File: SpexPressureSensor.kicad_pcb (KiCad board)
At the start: 2 copper layers, 28 x 28 mm, 28 parts, among them P1 CONN_6, P2 NICHROME, P3 TC2030-CTX, Q1 IRLL3303PbF, U1 ST1480ABDR, U2 TPS769XX, U3 MKL03ZxxVFG4, U4 BMP180, U7 LT6105

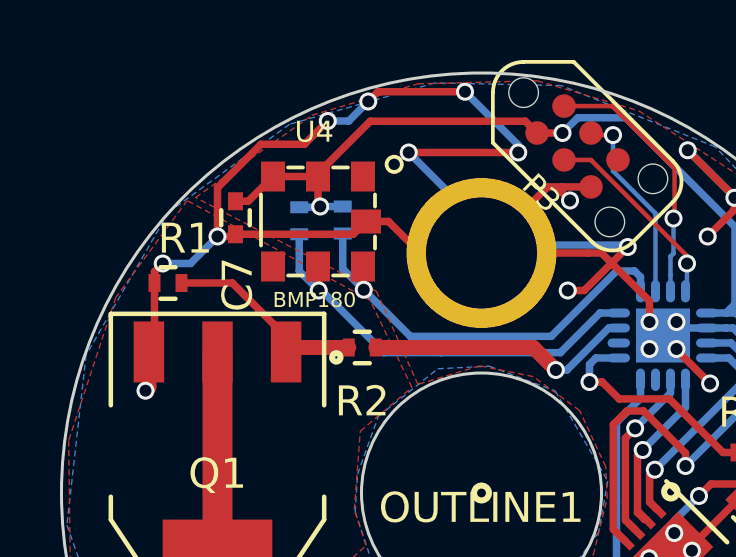
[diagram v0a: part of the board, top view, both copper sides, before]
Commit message: Changed the bmp180 for teh bme
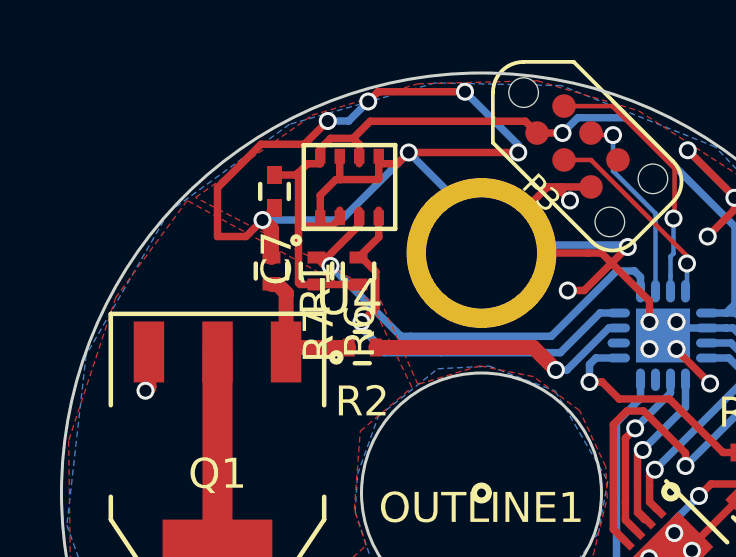
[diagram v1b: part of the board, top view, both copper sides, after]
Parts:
- C18: value C -> 1u
- R16, R18: value R -> 100
- R19: value R -> .02
- R20: value R -> 1000
- R6, R7: moved to F.Cu
- U4: value BMP180 -> BME280; footprint BMP180:LGA7-1.5-3.8X3.6MM -> bme280:LGA-8
- moved R1 3.47 mm to (113.0, 57.6), turned to 90 degrees
- moved R6 2.59 mm to (115.9, 57.6), turned to 90 degrees
- moved R7 1.91 mm to (114.5, 57.6), turned to 90 degrees
- moved C7 1.57 mm to (113.1, 55.0)
- moved U4 1.56 mm to (115.6, 54.8)
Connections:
- U4 pad 1: (no net) -> GND
- U4 pad 3: +3.3V -> Net-(R7-Pad2)
- U4 pad 4: (no net) -> Net-(R6-Pad2)
- U4 pad 5: Net-(R6-Pad2) -> GND
- U4 pad 6: Net-(R7-Pad2) -> +3.3V
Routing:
- net +3.3V: track 74.8 -> 79.3 mm, vias 6 -> 5
- net GND: track 204.3 -> 206.2 mm, vias 54 -> 53
- net Net-(Q1-Pad1): track 6.89 -> 5.24 mm
- net Net-(R7-Pad2): track 14.3 -> 15.7 mm

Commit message: Fixed some issues
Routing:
- net +3.3V: track 79.3 -> 79.8 mm
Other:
- outline, holes or cut-outs redrawn
